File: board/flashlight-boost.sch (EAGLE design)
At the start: 15 parts

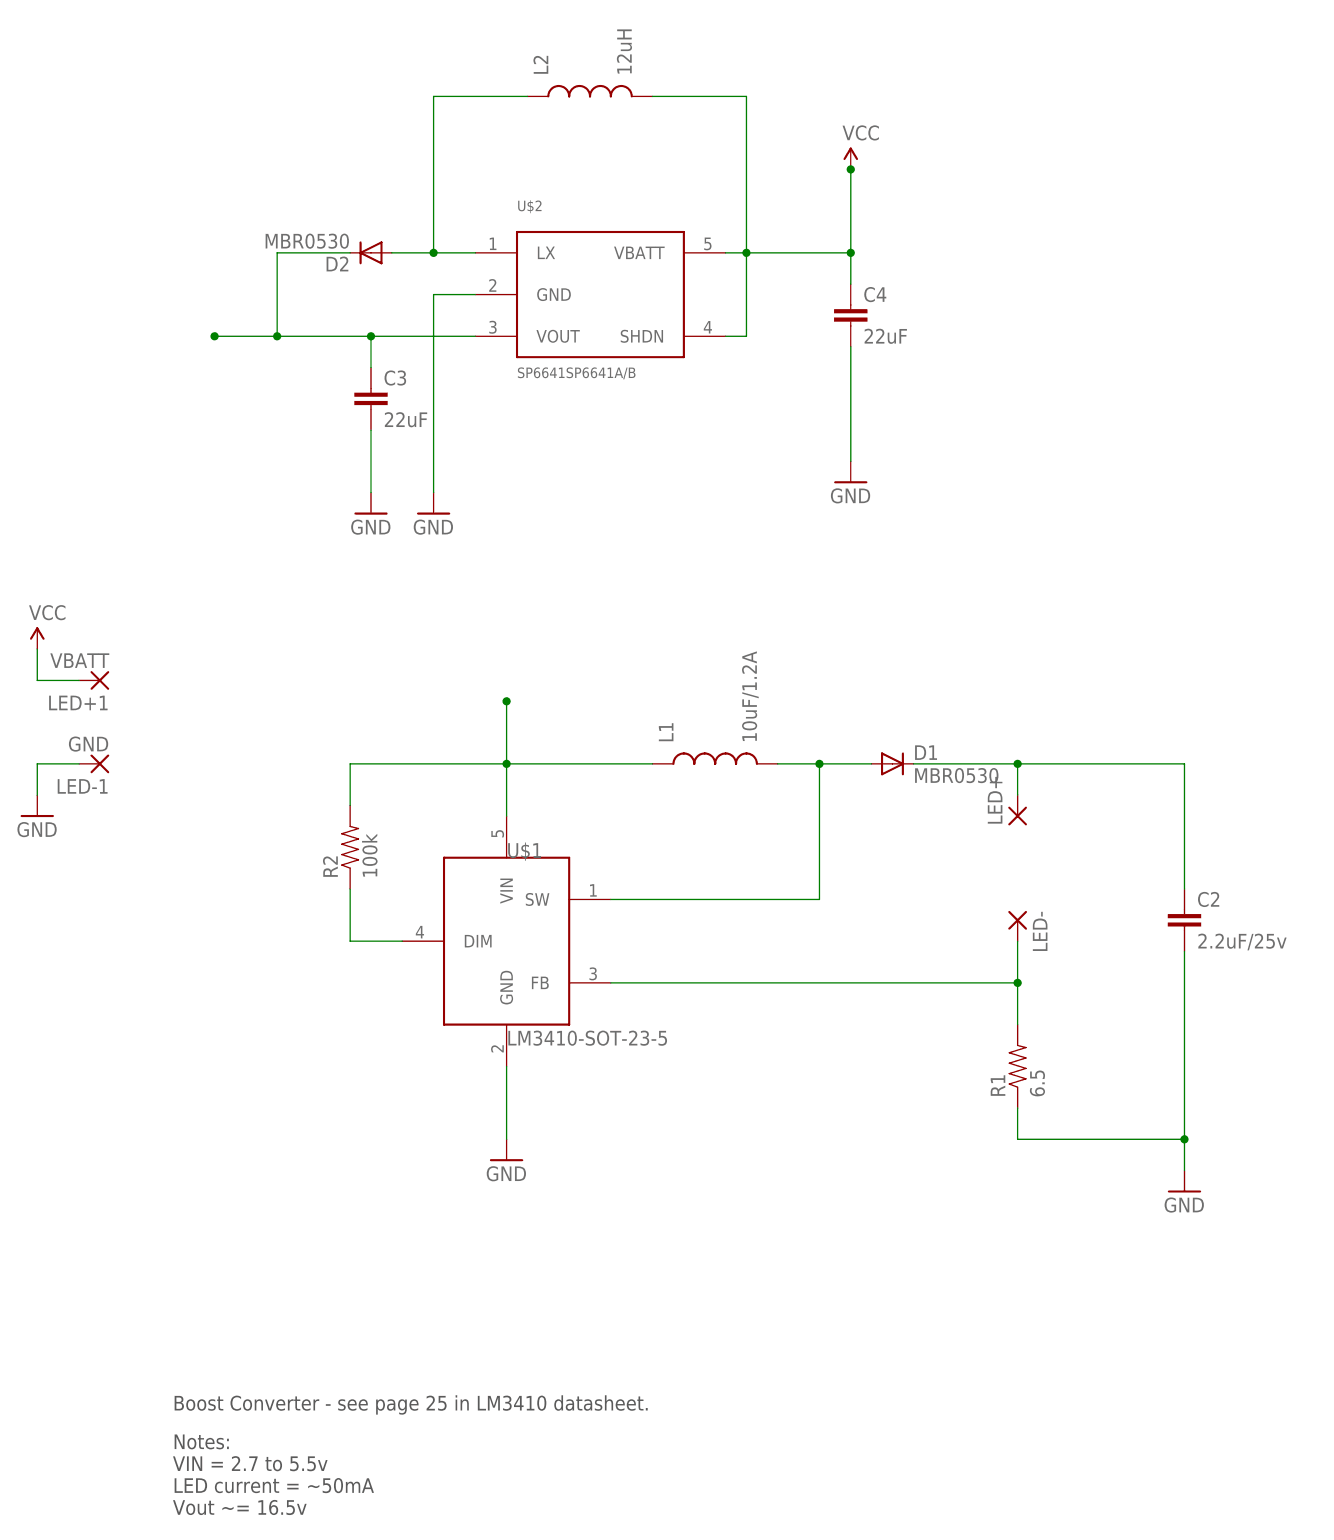
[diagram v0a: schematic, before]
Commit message: removing constant current LED driver since the current sense resistor for it is the same value as the LED series resistor
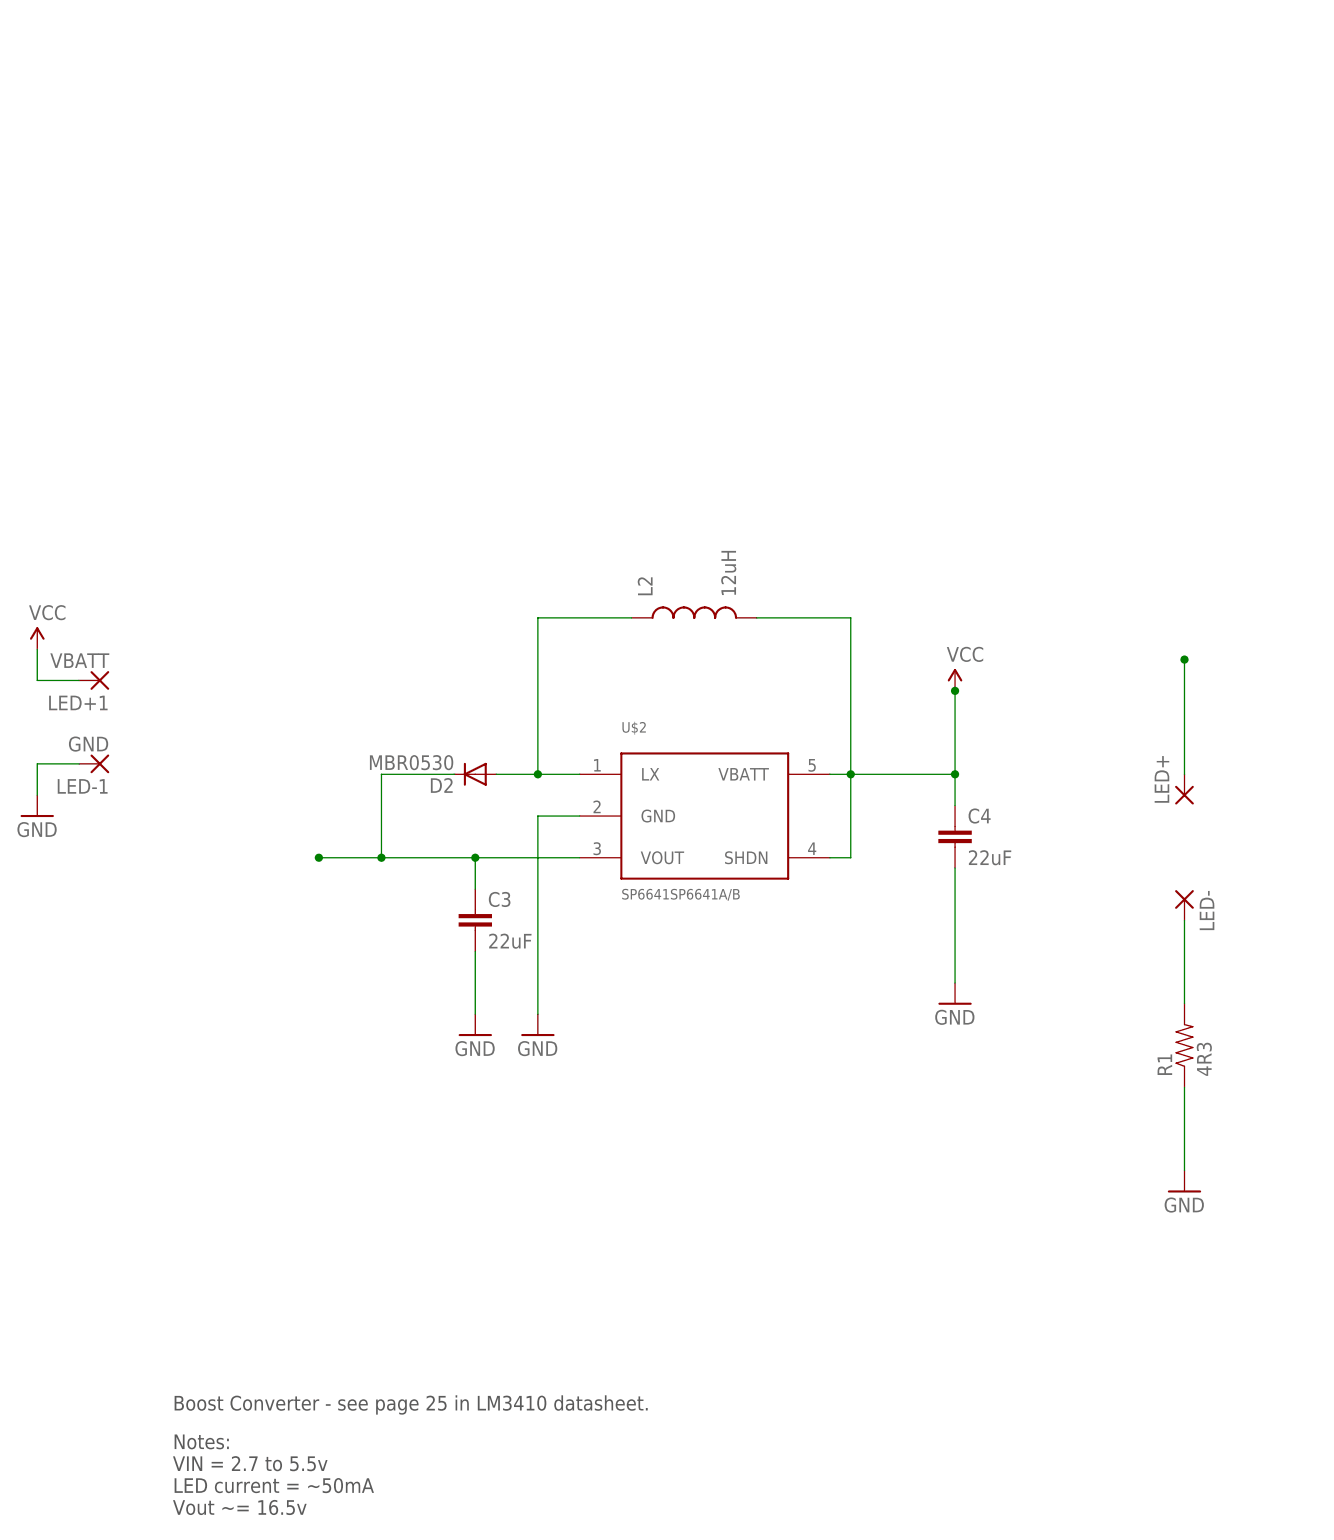
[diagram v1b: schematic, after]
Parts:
- removed C2: 2.2uF/25v, SparkFun-Passives:CAP1206
- removed D1: MBR0530, diode:MBR0520LT
- removed L1: 10uF/1.2A, SparkFun-Passives:INDUCTOR1210
- removed R2: 100k, SparkFun-Resistors:RESISTOR0603-RES
- removed U$1: LM3410-SOT-23-5, Synapseware:LM3410-SOT-23-5
- R1: value 6.5 -> 4R3
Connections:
- removed net DIM: R2.1, U$1.DIM
- removed net N$10: C2.1, D1.C, LED+.P
- removed net N$2: D1.A, L1.2, U$1.SW
- net GND: no longer C2.2, U$1.GND
- net N$7: no longer U$1.FB
- net VSUPPLY: now also LED+.P; no longer L1.1, R2.2, U$1.VIN
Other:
- moved on the sheet: C3, C4, D2, L2, LED+, LED-, R1, U$2

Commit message: misc updates
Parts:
- L2: value 12uH -> 22uH
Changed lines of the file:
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@@
 <setting verticaltext="up"/>
 </settings>
-<grid distance="0.1" unitdist="inch" unit="inch" style="lines" multiple="1" display="no" altdistance="0.01" altunitdist="inch" altunit="inch"/>
+<grid distance="0.05" unitdist="inch" unit="inch" style="lines" multiple="1" display="yes" altdistance="0.005" altunitdist="inch" altunit="inch"/>
 <layers>
 <layer number="1" name="Top" color="4" fill="1" visible="no" active="no"/>
@@
 <part name="LED-1" library="wirepad" deviceset="2,54/1,0" device="" value="GND"/>
 <part name="U$2" library="Sipex Custom" deviceset="SP6641" device="SP6641A/B"/>
-<part name="L2" library="SparkFun-Passives" deviceset="INDUCTOR" device="1210" value="12uH"/>
+<part name="L2" library="SparkFun-Passives" deviceset="INDUCTOR" device="1210" value="22uH"/>
 <part name="D2" library="diode" deviceset="MBR0520LT" device="" value="MBR0530"/>
 <part name="C3" library="SparkFun-Passives" deviceset="CAP" device="1206" value="22uF"/>

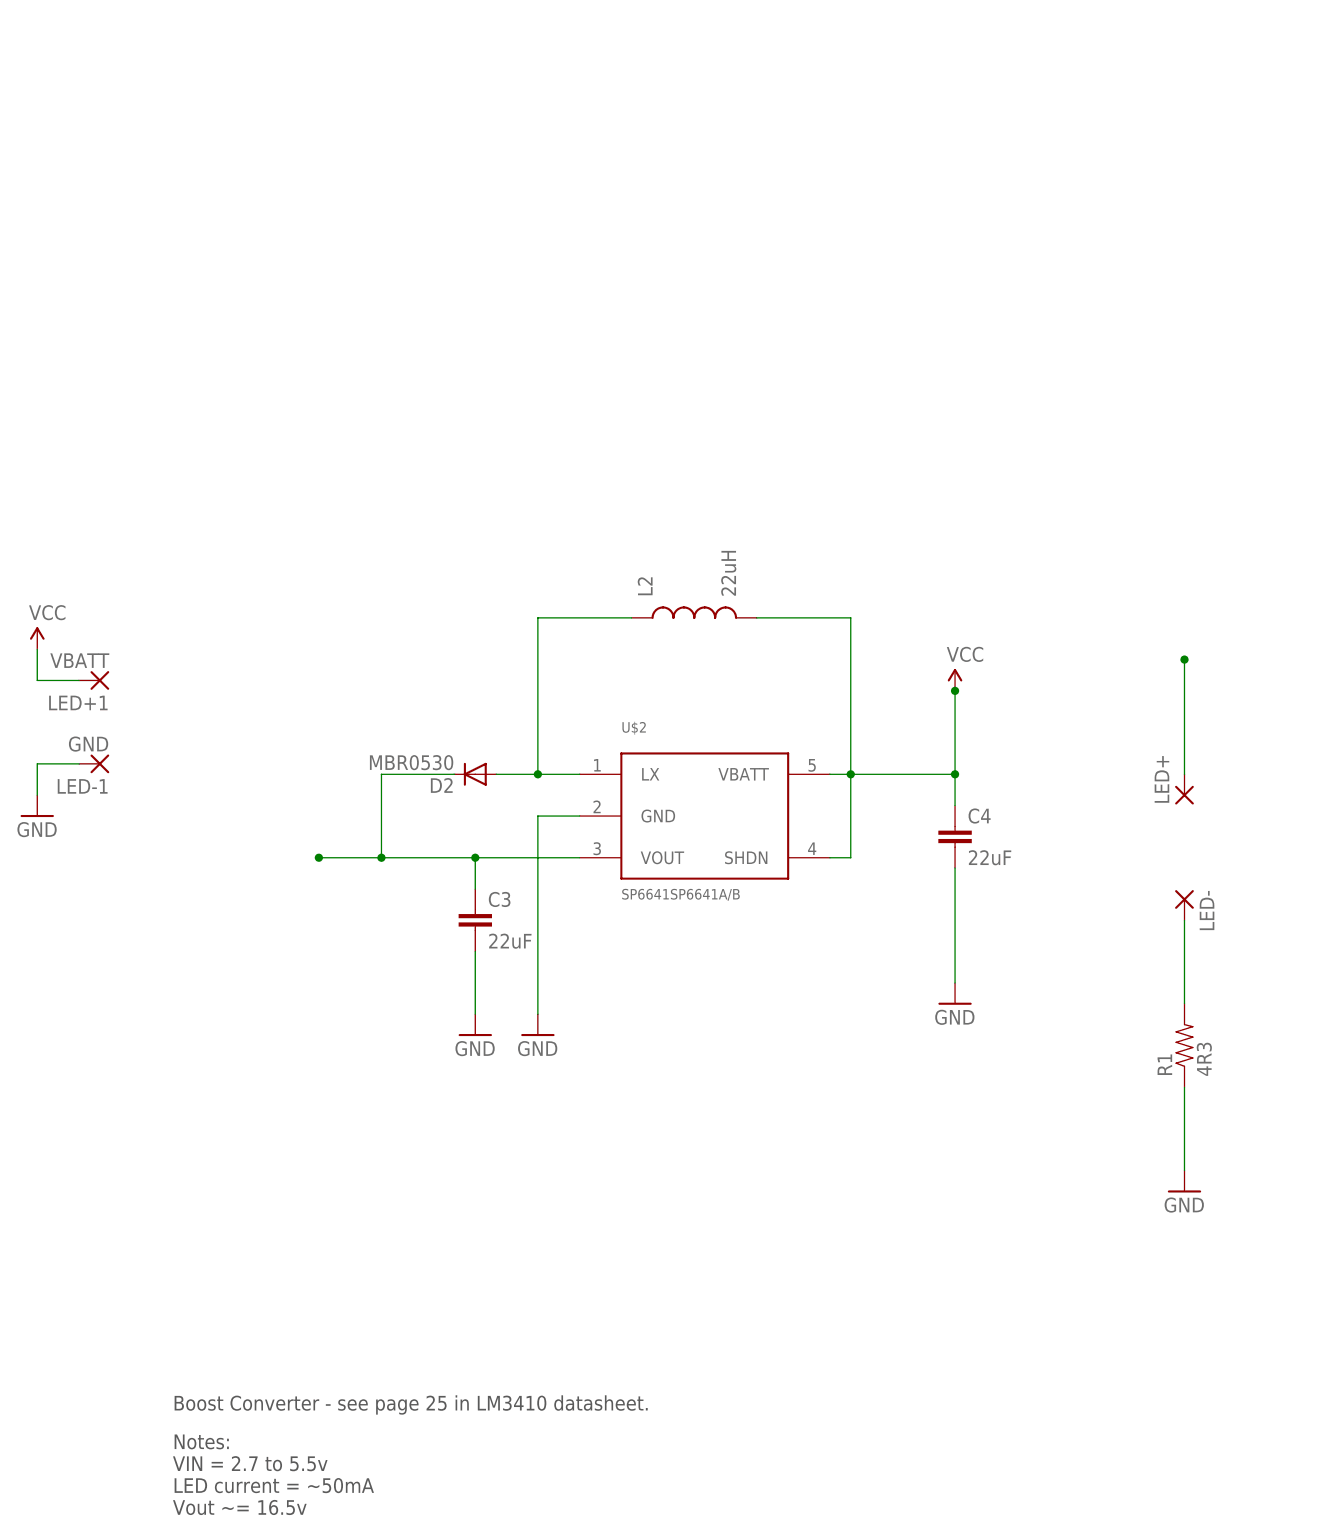
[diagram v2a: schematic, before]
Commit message: Converting driver board to use LTC3490 part
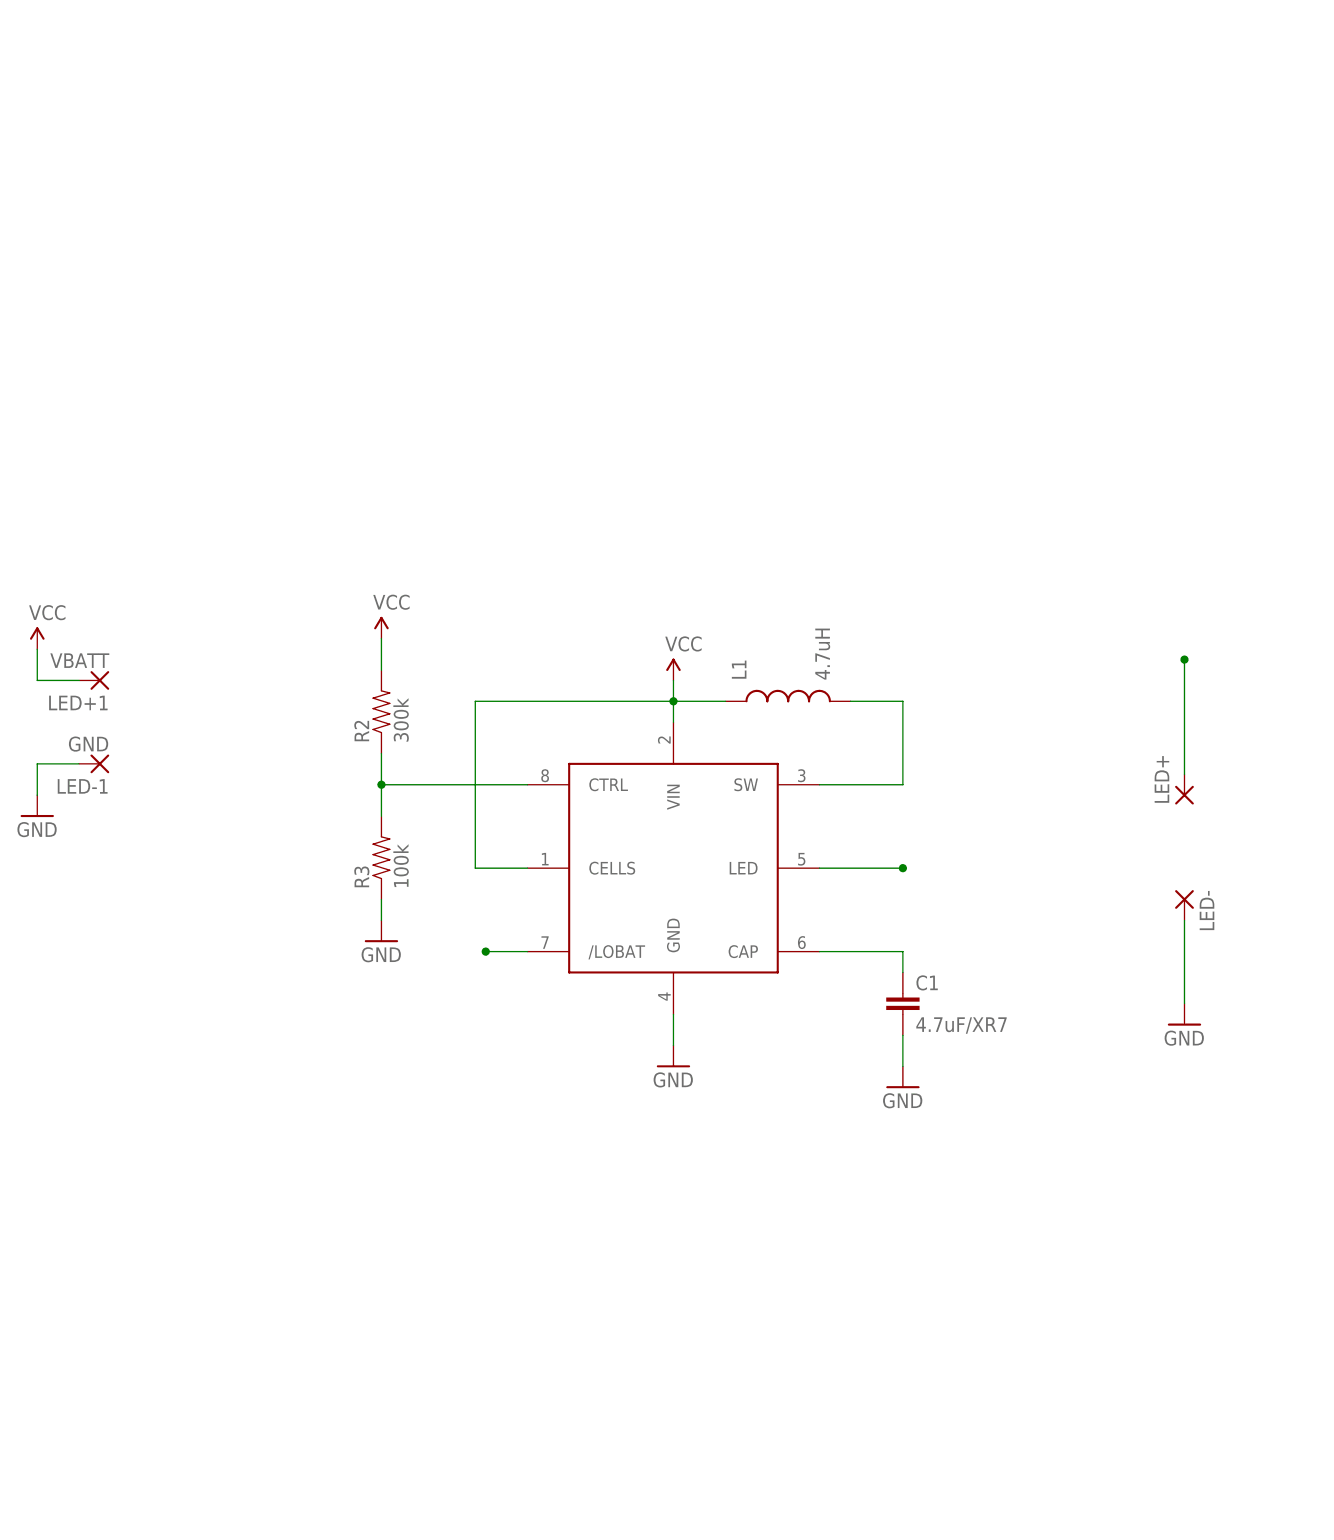
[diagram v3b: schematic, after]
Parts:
- removed C3, C4: 22uF, SparkFun-Passives:CAP1206
- removed D2: MBR0530, diode:MBR0520LT
- removed L2: 22uH, SparkFun-Passives:INDUCTOR1210
- removed R1: 4R3, SparkFun-Resistors:RESISTOR1206
- removed U$2: SP6641SP6641A/B, Sipex Custom:SP6641SP6641A/B
- added C1: 4.7uF/XR7, SparkFun-Passives:CAP1206
- added L1: 4.7uH, SparkFun-Passives:INDUCTOR1210
- added R2: 300k, SparkFun-Resistors:RESISTOR0603-RES
- added R3: 100k, SparkFun-Resistors:RESISTOR0603-RES
- added U$1: LTC3490NSOIC-8, Synapseware:LTC3490NSOIC-8
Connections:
- removed net N$7: LED-.P, R1.2
- removed net N$9: D2.A, L2.1, U$2.LX
- removed net VSUPPLY: C3.1, D2.C, LED+.P, U$2.VOUT
- new net LED: LED+.P, U$1.LED
- new net N$10: R2.1, R3.2, U$1.CTRL
- new net N$4: L1.2, U$1.SW
- new net N$5: C1.1, U$1.CAP
- new net N$6: U$1./LOBAT
- net GND: now also C1.2, LED-.P, R3.1, U$1.GND; no longer C3.2, C4.2, R1.1, U$2.GND
- net VCC: now also L1.1, R2.2, U$1.CELLS, U$1.VIN; no longer C4.1, L2.2, U$2.SHDN, U$2.VBATT
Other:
- note removed: "Boost Converter - see page 25 in LM3410 datasheet."
- note removed: "Notes: VIN = 2.7 to 5.5v LED current = ~50mA Vout ~= 16.5v"
